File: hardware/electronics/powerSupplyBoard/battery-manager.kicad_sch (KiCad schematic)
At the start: 47 parts, among them J5 1726480102, J6 S3B-XH-SM4-TB, Q2 BUK6D72-30EX, Q3 NXV90EP, Q4 BUK6D72-30EX, Q5 2N7002NXAK, U4 BQ40Z50-R2

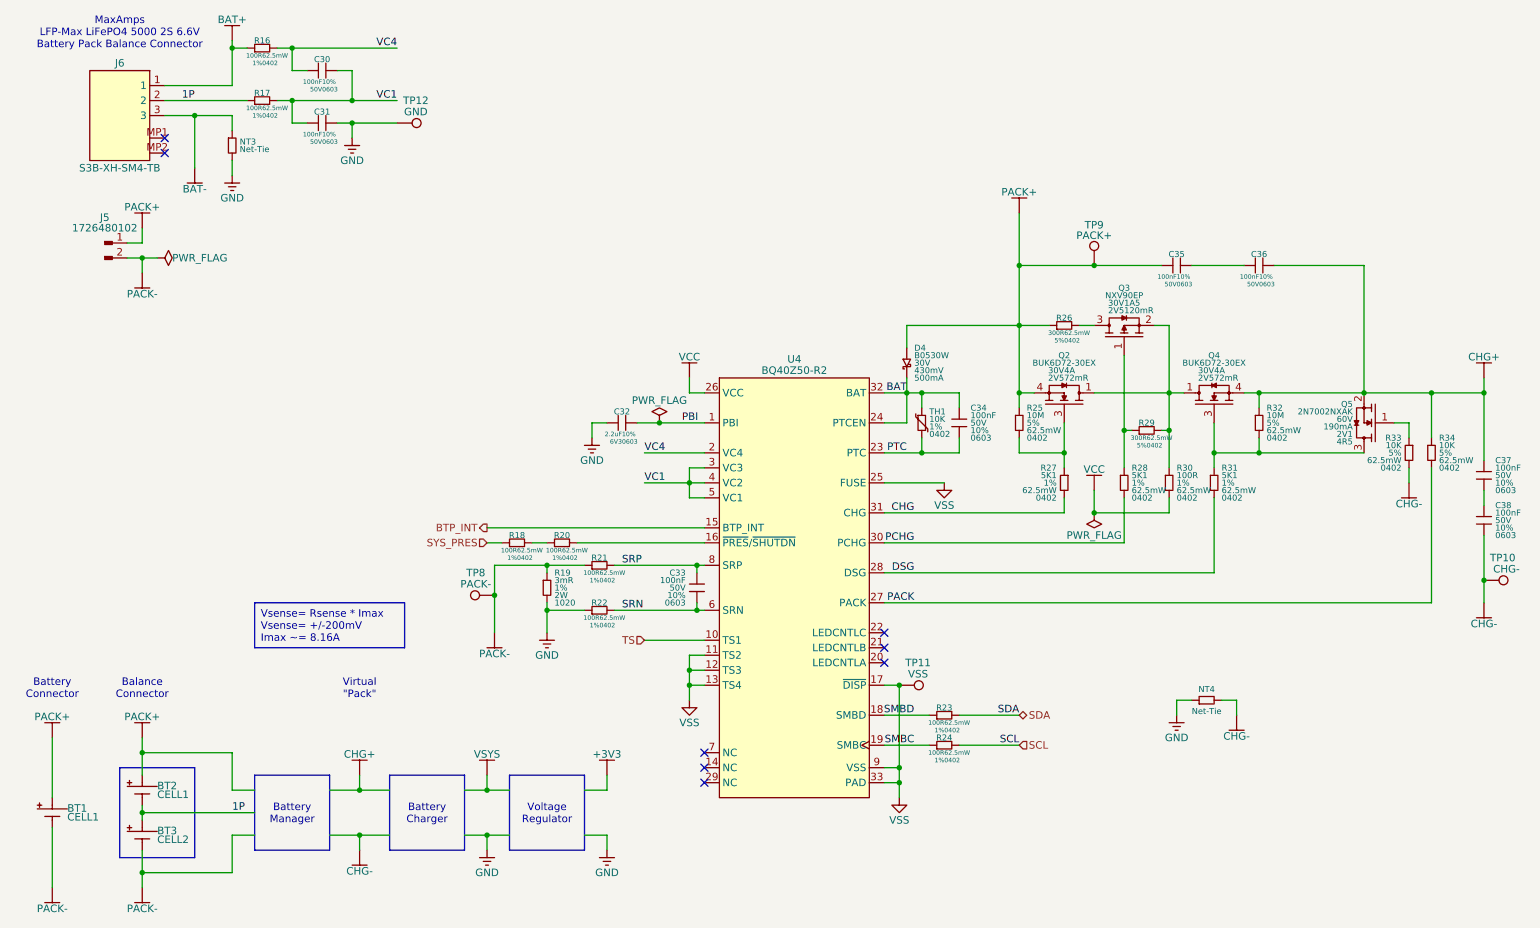
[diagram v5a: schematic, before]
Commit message: fixed power nets
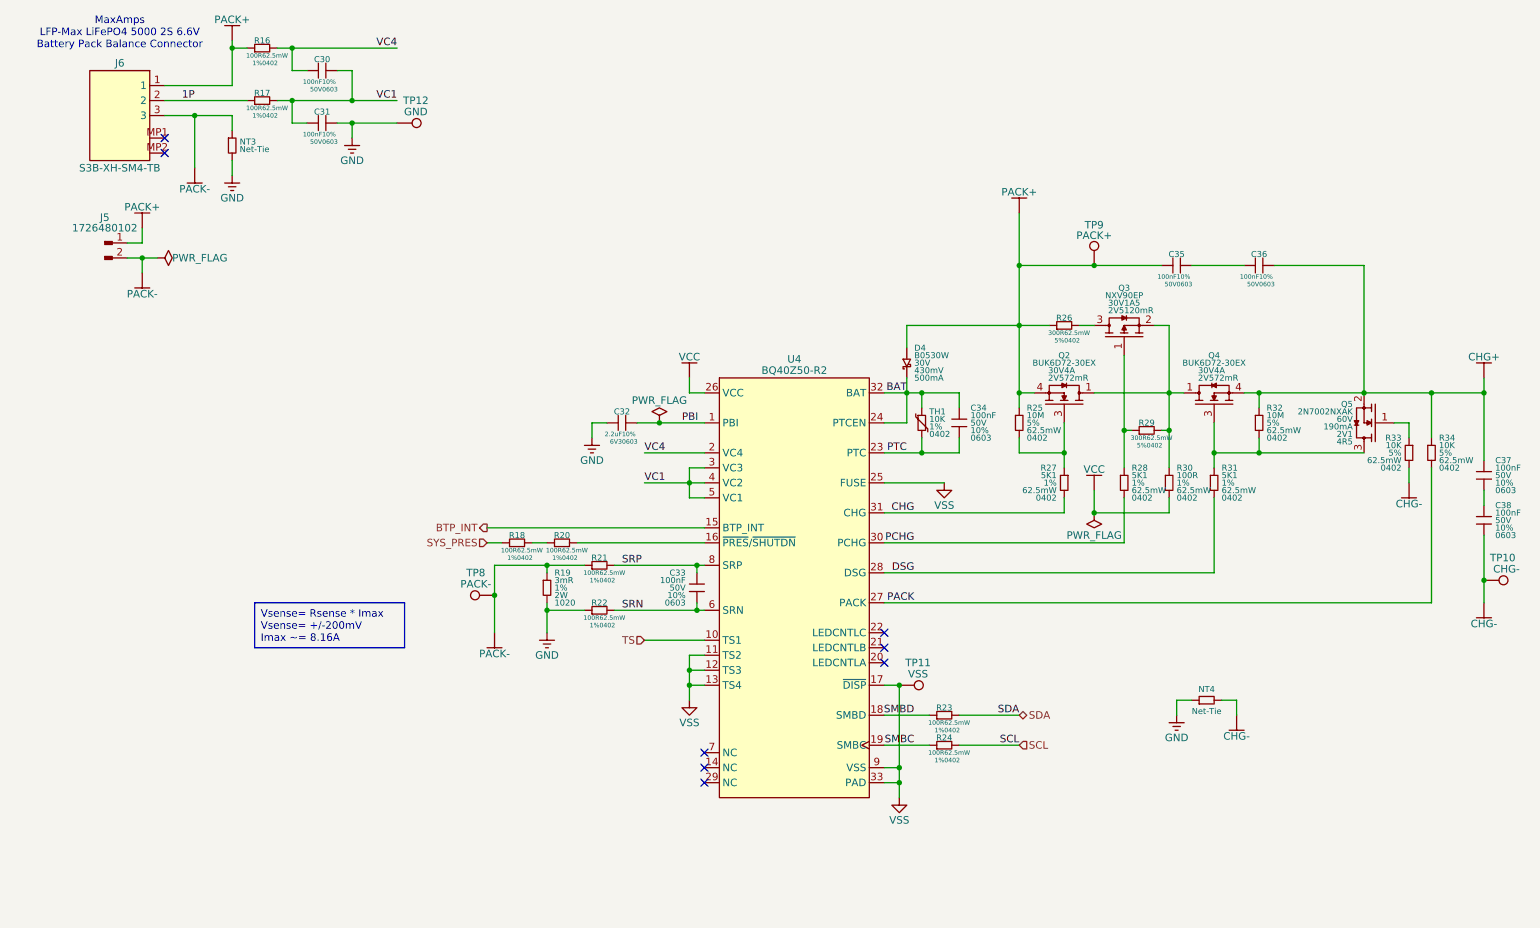
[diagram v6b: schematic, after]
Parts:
- removed BT1, BT2, BT3: ~, symbol DS-Batteries:Battery
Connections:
- net BAT+ is gone; now on net PACK+: J6.1, R16.1
- net BAT- is gone; now on net PACK-: J6.3, NT3.1
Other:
- note removed: "Balance Connector"
- note removed: "Battery Connector"
- note removed: "Virtual "Pack""

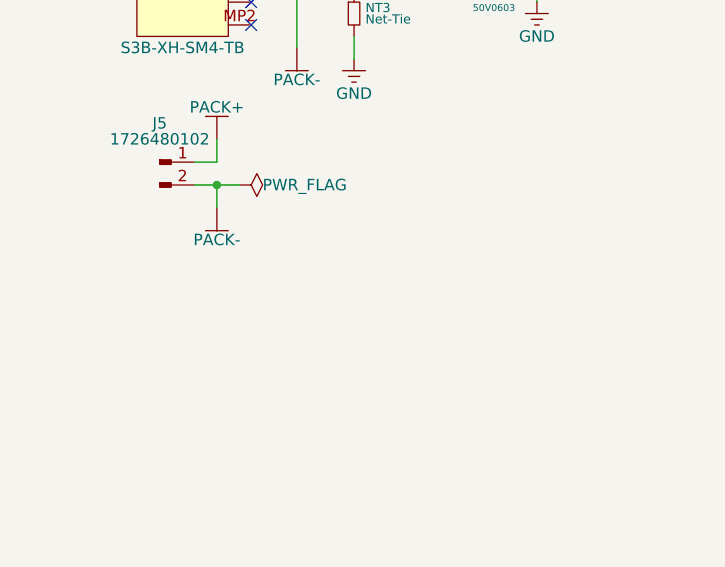
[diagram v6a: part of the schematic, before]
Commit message: fixed design review changes (power nets)
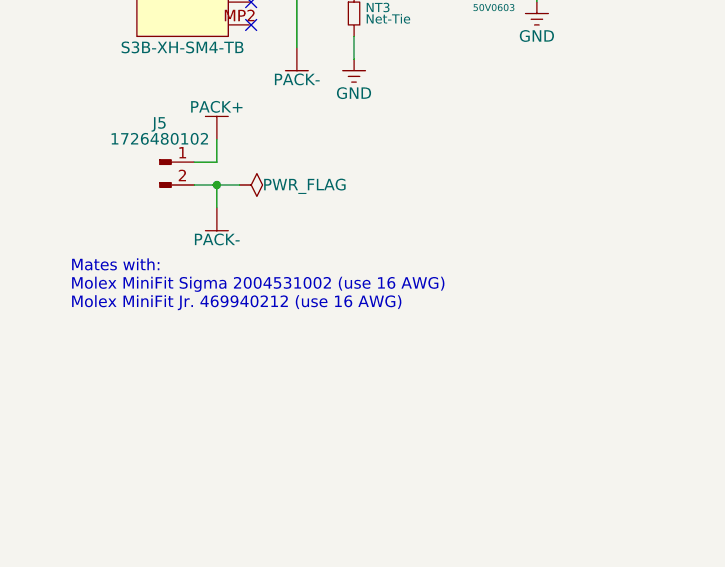
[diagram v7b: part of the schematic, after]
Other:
- note added: "Mates with: Molex MiniFit Sigma 2004531002 (use 16 AWG) Molex MiniFit Jr. 469940212 (use 16 AWG)"
